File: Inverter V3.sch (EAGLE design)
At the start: 67 parts, among them IC1 LTV-816, IC2 LTV-816, IC3 LTV-816, IC4 LTV-816, IC5 LTV-816, IC6 LTV-816, Q1 ROHM_SCT3022ALGC11ROHM_SCT302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, Q2 ROHM_SCT3022ALGC11ROHM_SCT302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, Q3 ROHM_SCT3022ALGC11ROHM_SCT302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, Q4 ROHM_SCT3022ALGC11ROHM_SCT302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, Q5 ROHM_SCT3022ALGC11ROHM_SCT302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, Q6 ROHM_SCT3022ALGC11ROHM_SCT302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, U1 RASPBERRY_PICOTH

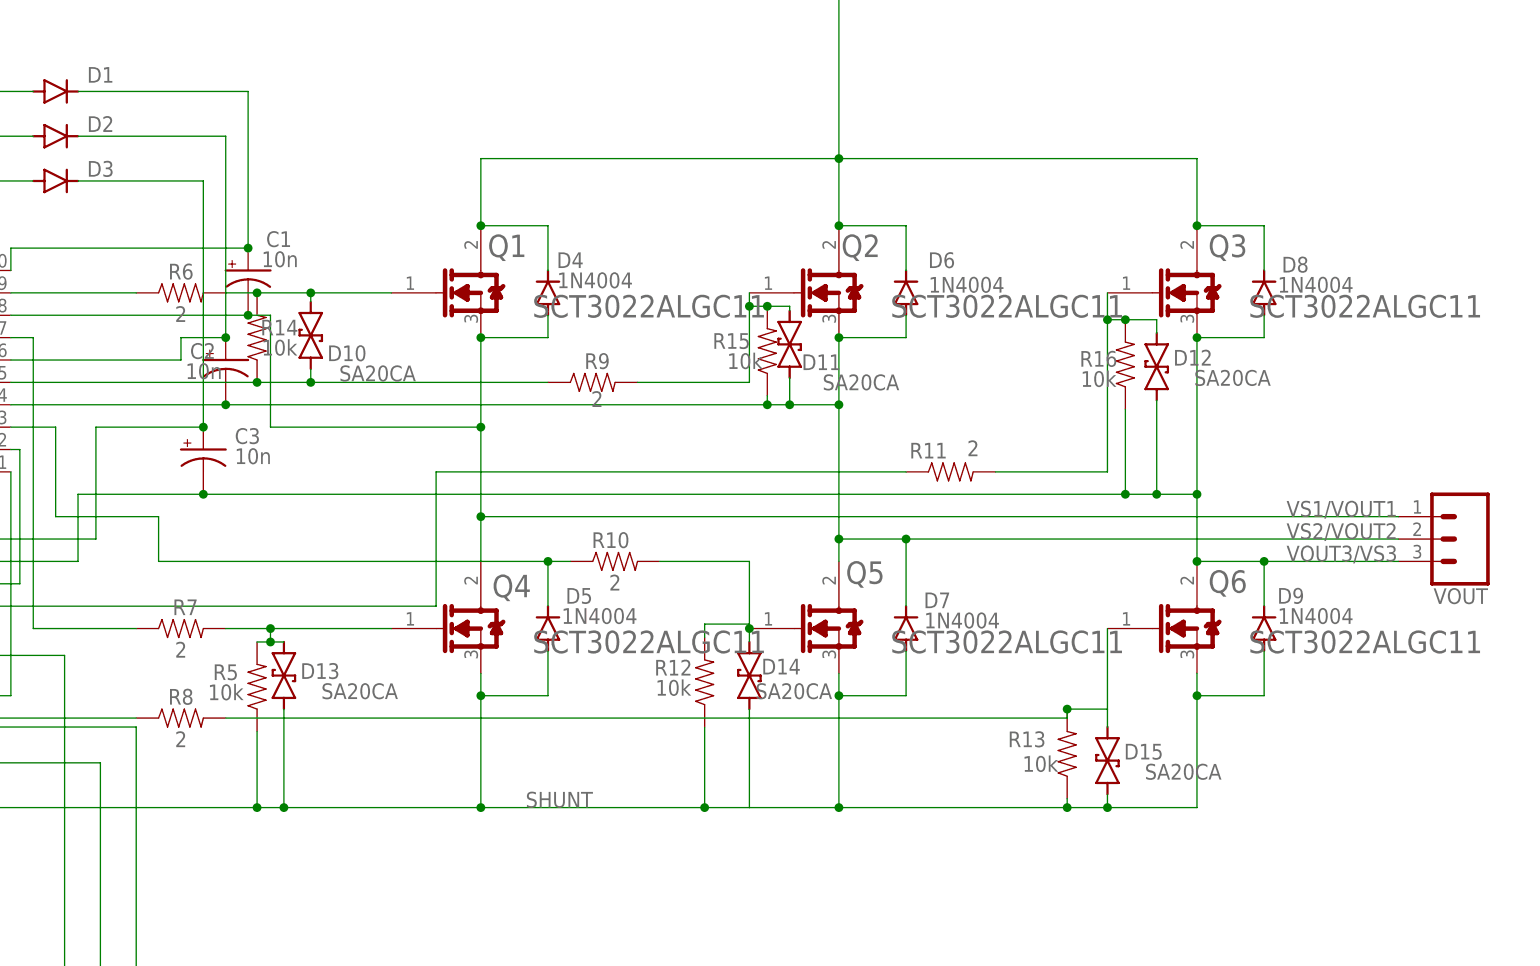
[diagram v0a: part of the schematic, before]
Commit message: Swapped flyback diodes and added silkscreen for IC pins
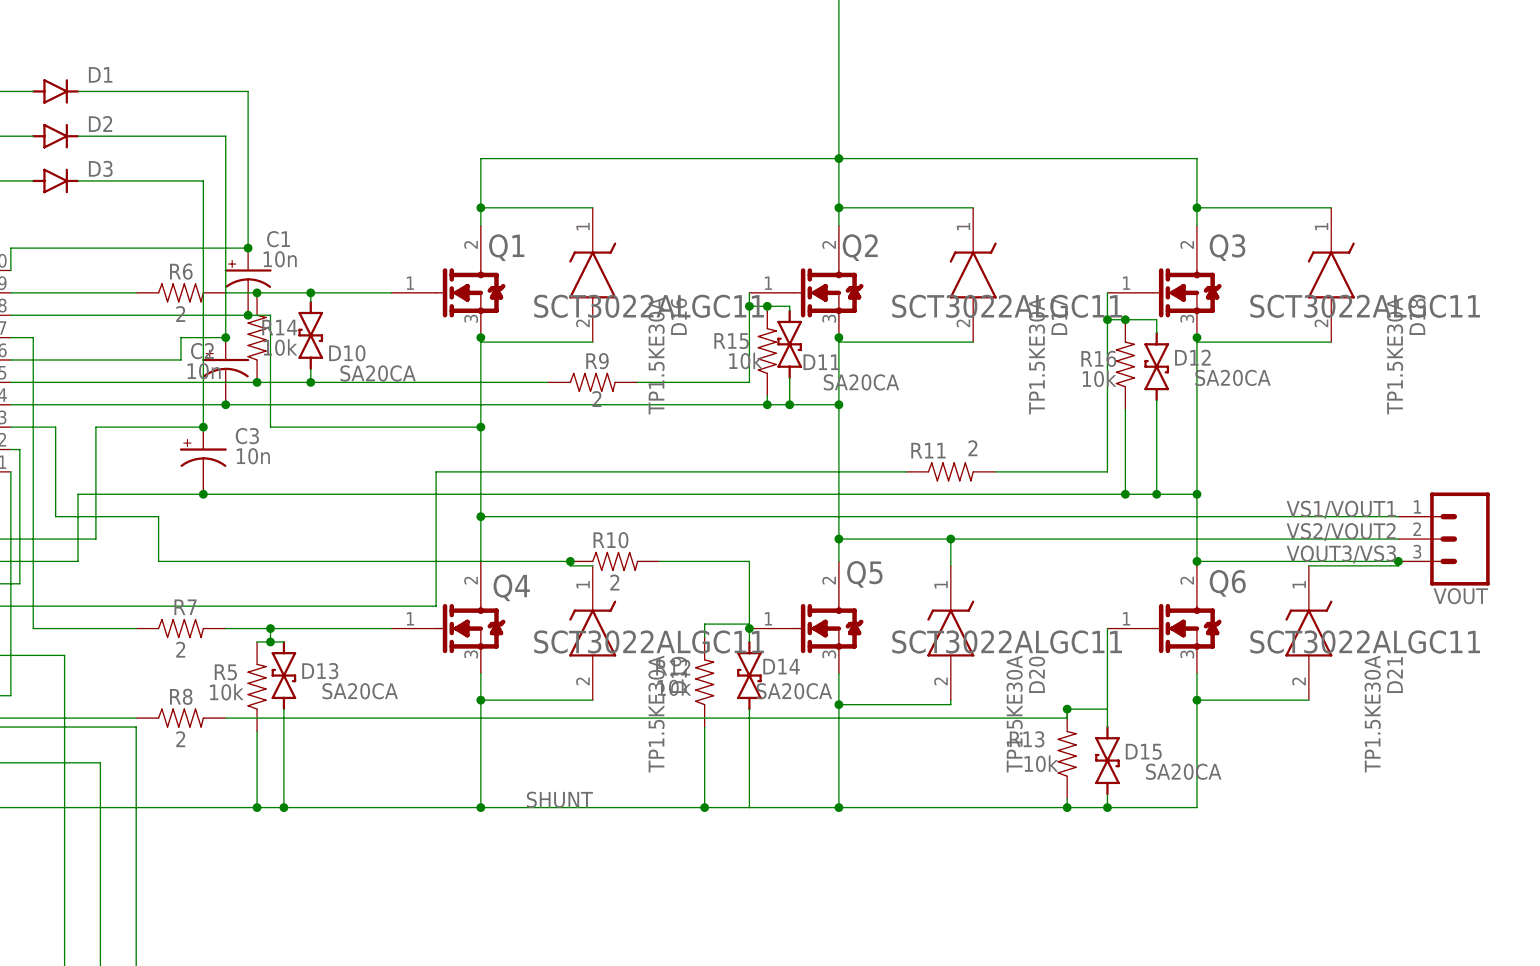
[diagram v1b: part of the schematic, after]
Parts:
- removed D4, D5, D6, D7, D8, D9: 1N4004, diode:1N4004
- added D16, D17, D18, D19, D20, D21: TP1.5KE30A, TP1.5KE30A:TP1.5KE30A
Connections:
- net LO2: now also D19.K; no longer D5.C
- net SHUNT: now also D19.A, D20.A, D21.A; no longer D5.A, D7.A, D9.A
- net V+: now also D16.K, D17.K, D18.K; no longer D4.C, D6.C, D8.C
- net VOUT3/VS3: now also D18.A, D21.K; no longer D8.A, D9.C
- net VS1/VOUT1: now also D16.A; no longer D4.A
- net VS2/VOUT2: now also D17.A, D20.K; no longer D6.A, D7.C
